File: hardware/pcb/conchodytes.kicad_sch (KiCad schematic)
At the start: 0 parts

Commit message: élagage des feuilles + réparation des tables de bibliothèques
Mae a élagué dans l'éditeur :
- mcu  : 108 -> 16 composants. Restent le S3, le nRF24, leurs découplages, le
  connecteur de prog et les 100 ohms. Partis : la matrice 26 switchs / 24
  diodes, les 11 TVS, le TRRS, l'écran, le trackpad.
- usbc : 6 -> 4 composants. Le hub CH334R (U53) est parti, il venait du coffre
  P4 et n'avait rien à faire dans une souris. Restent J48, U54 (USBLC6) et les
  deux 5k1 de CC.

Tables de bibliothèques réparées : elles pointaient vers des fichiers absents ou
renommés (optical mouse.lib -> optical_mouse.lib, nice_nano, RP2040, SSD1306).
Mouse.pretty rapatrié du fork : les 6 empreintes de la coque en dépendent.

ERC : 96 -> 24 violations.

Co-Authored-By: Claude Opus 5 <noreply@anthropic.com>
Claude-Session: https://claude.ai/code/session_01GfX5RmekmQi78Dm37qsT4Z
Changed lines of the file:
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@@
 		)
 		(property "Sheetname" "power"
-			(at 25.4 24.688399999999998 0)
+			(at 25.4 24.6884 0)
 			(show_name no)
 			(do_not_autoplace no)
@@
 		(instances
 			(project "conchodytes"
-				(path "/11111111-2222-3333-4444-00000000000f"
+				(path "/7138aad8-3c5f-41d0-9987-adc2f08f0576"
 					(page "2")
 				)
@@
 		)
 		(property "Sheetfile" "usbc.kicad_sch"
-			(at 25.4 59.096199999999996 0)
+			(at 25.4 59.0962 0)
 			(show_name no)
 			(do_not_autoplace no)
@@
 		(instances
 			(project "conchodytes"
-				(path "/11111111-2222-3333-4444-00000000000f"
+				(path "/7138aad8-3c5f-41d0-9987-adc2f08f0576"
 					(page "3")
 				)
@@
 		(instances
 			(project "conchodytes"
-				(path "/11111111-2222-3333-4444-00000000000f"
+				(path "/7138aad8-3c5f-41d0-9987-adc2f08f0576"
 					(page "4")
 				)
@@
 			(page "1")
 		)
-		(path "/11111111-2222-3333-4444-000000000003"
-			(page "4")
-		)
-		(path "/11111111-2222-3333-4444-000000000001"
-			(page "2")
-		)
-		(path "/11111111-2222-3333-4444-000000000002"
-			(page "3")
-		)
 	)

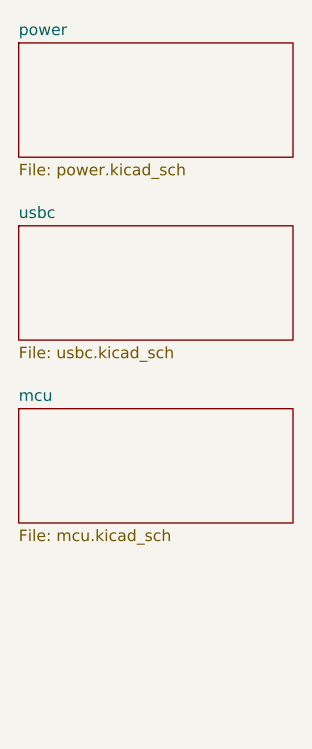
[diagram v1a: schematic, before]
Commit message: feuille sensor + correction de mon analyse de la radio
La liaison S3 <-> nRF24 est intacte : je l'avais lue comme cassée alors que
chaque ligne passe par sa résistance série de 100 ohms, nommée localement d'un
côté (SCK_L / MOSI_L / MISO_L) et anonyme de l'autre. Rien à réparer :
  U8.5 SCK  -R30- U6.31 (GPIO38)   U8.4 CSN -R36- U6.9  (GPIO16)
  U8.6 MOSI -R18- U6.33 (GPIO40)   U8.3 CE  -R39- U6.8  (GPIO15)
  U8.7 MISO -R16- U6.32 (GPIO39)   U8.8 IRQ -R41- U6.34 (GPIO41)

Ajout de sensor.kicad_sch, cinquième feuille de la hiérarchie, avec la liste de
ce qui doit y être posé et les références exactes à respecter — SW1/SW2/SW3,
LD1/LQ1, U2 — pour que le F8 retrouve les empreintes verrouillées du PCB.

Les 20 GPIO libérés par le retrait de la matrice apparaissent maintenant en
pin_not_connected : c'est attendu, ils attendent le câblage du capteur.

Note : j'ai tenté de poser le PWR_FLAG du +5V par script, sans succès — le
symbole n'atterrissait pas sur le net. Revert. À poser dans l'éditeur.

Co-Authored-By: Claude Opus 5 <noreply@anthropic.com>
Claude-Session: https://claude.ai/code/session_01GfX5RmekmQi78Dm37qsT4Z
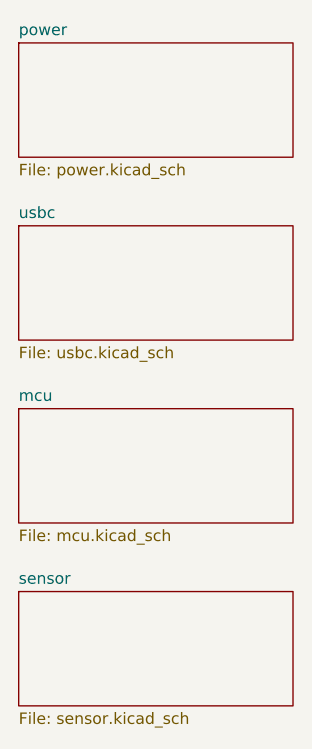
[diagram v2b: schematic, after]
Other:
- added sheet sensor (sensor.kicad_sch)
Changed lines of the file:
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@@
+		)
+	)
+	(sheet
+		(at 25.4 86.36)
+		(size 30.48 12.7)
+		(exclude_from_sim no)
+		(in_bom yes)
+		(on_board yes)
+		(dnp no)
+		(fields_autoplaced yes)
+		(stroke
+			(width 0.1524)
+			(type solid)
+		)
+		(fill
+			(color 0 0 0 0)
+		)
+		(property "Sheetname" "sensor"
+			(at 25.4 85.6484 0)
+			(show_name no)
+			(do_not_autoplace no)
+			(effects
+				(font
+					(size 1.27 1.27)
+				)
+				(justify left bottom)
+			)
+		)
+		(property "Sheetfile" "sensor.kicad_sch"
+			(at 25.4 99.7362 0)
+			(show_name no)
+			(do_not_autoplace no)
+			(effects
+				(font
+					(size 1.27 1.27)
+				)
+				(justify left top)
+			)
+		)
+		(instances
+			(project "conchodytes"
+				(path "/11111111-2222-3333-4444-00000000000f"
+					(page "5")
+				)
+			)
 		)
 	)
@@
 			(page "1")
 		)
+		(path "/11111111-2222-3333-4444-000000000004"
+			(page "5")
+		)
 	)
